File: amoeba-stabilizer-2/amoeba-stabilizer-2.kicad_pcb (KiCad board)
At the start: 2 copper layers, 35.1 x 20.8 mm, 29 parts

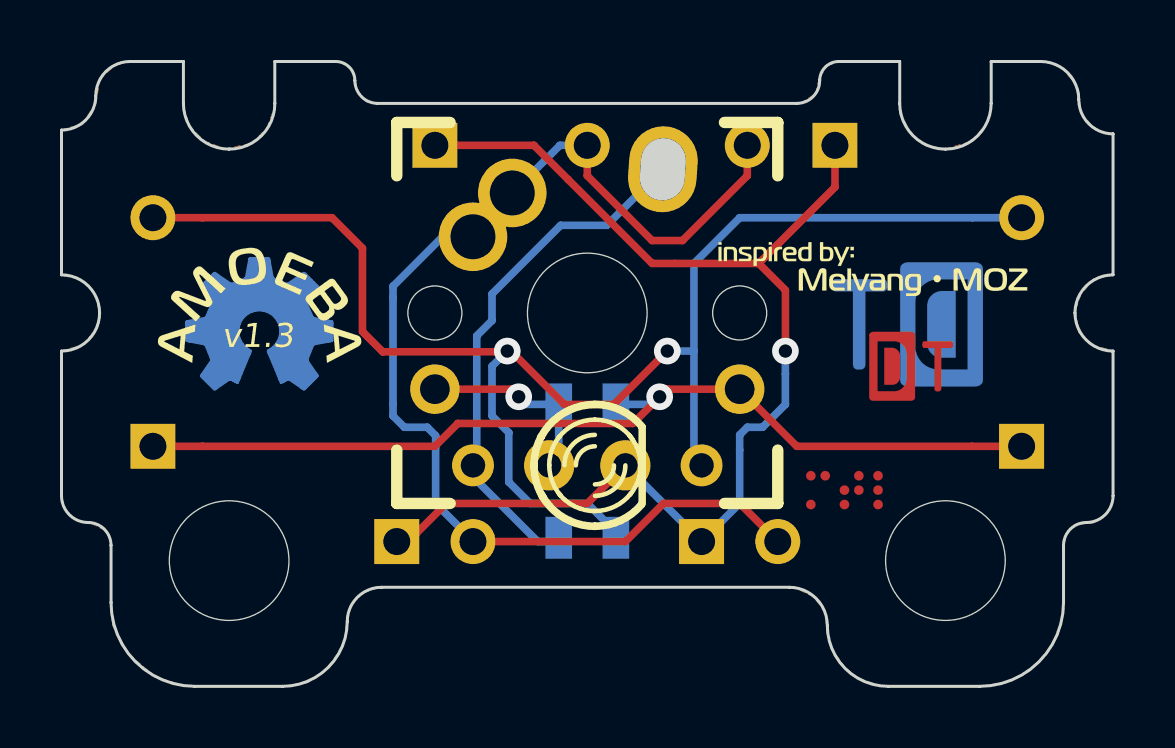
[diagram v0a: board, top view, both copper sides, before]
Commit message: Tighten solder masks, add pad arrows to amoeba-stabilizer-2, convert amoeba on 2u to copper.
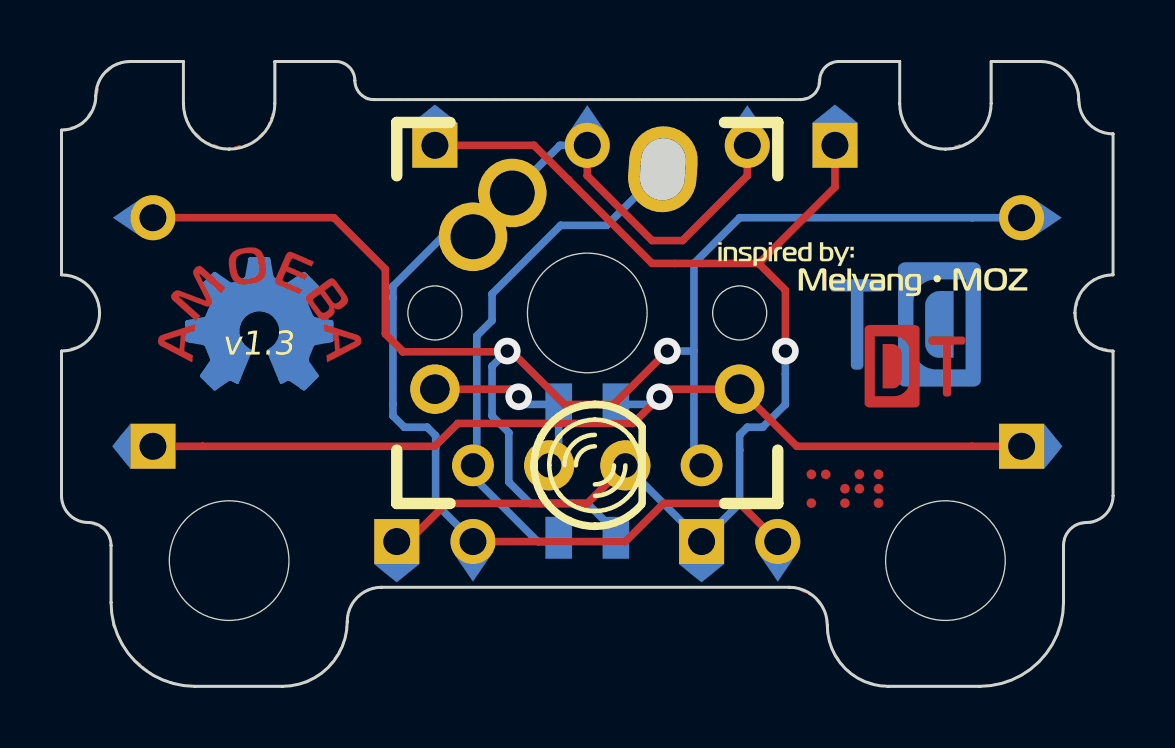
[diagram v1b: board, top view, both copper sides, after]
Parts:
- removed amoeba-round: G***, amoeba-round
- removed dt-logo: G***, dt-logo
- added amoeba-round-cu: G***, amoeba-round-cu, F.Cu at (238.0, 110.2)
- added dt-logo-d: G***, dt-logo-d, F.Cu at (259.1, 112.1)
- added dt-logo-t: G***, dt-logo-t, F.Cu at (260.9, 112.2)
- added pad-arrow-round: G***, pad-arrow-round, B.Cu at (255.3, 118.4)
- added pad-arrow-round: G***, pad-arrow-round, B.Cu at (245.1, 118.4)
- added pad-arrow-round: G***, pad-arrow-round, B.Cu at (234.1, 107.3)
- added pad-arrow-round: G***, pad-arrow-round, B.Cu at (263.7, 107.3)
- added pad-arrow-round: G***, pad-arrow-round, B.Cu at (254.3, 104.6)
- added pad-arrow-round: G***, pad-arrow-round, B.Cu at (248.9, 104.6)
- added pad-arrow-square: G***, pad-arrow-square, B.Cu at (243.8, 104.6)
- added pad-arrow-square: G***, pad-arrow-square, B.Cu at (257.2, 104.6)
- added pad-arrow-square: G***, pad-arrow-square, B.Cu at (263.7, 114.9)
- added pad-arrow-square: G***, pad-arrow-square, B.Cu at (252.7, 118.4)
- added pad-arrow-square: G***, pad-arrow-square, B.Cu at (242.6, 118.4)
- added pad-arrow-square: G***, pad-arrow-square, B.Cu at (234.1, 114.9)
- moved mtl-braille 0.14 mm to (257.4, 116.3)
- moved dt-logo-big-rev 0.06 mm to (259.5, 110.9)
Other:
- outline, holes or cut-outs redrawn

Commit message: Replaced OSH logo.
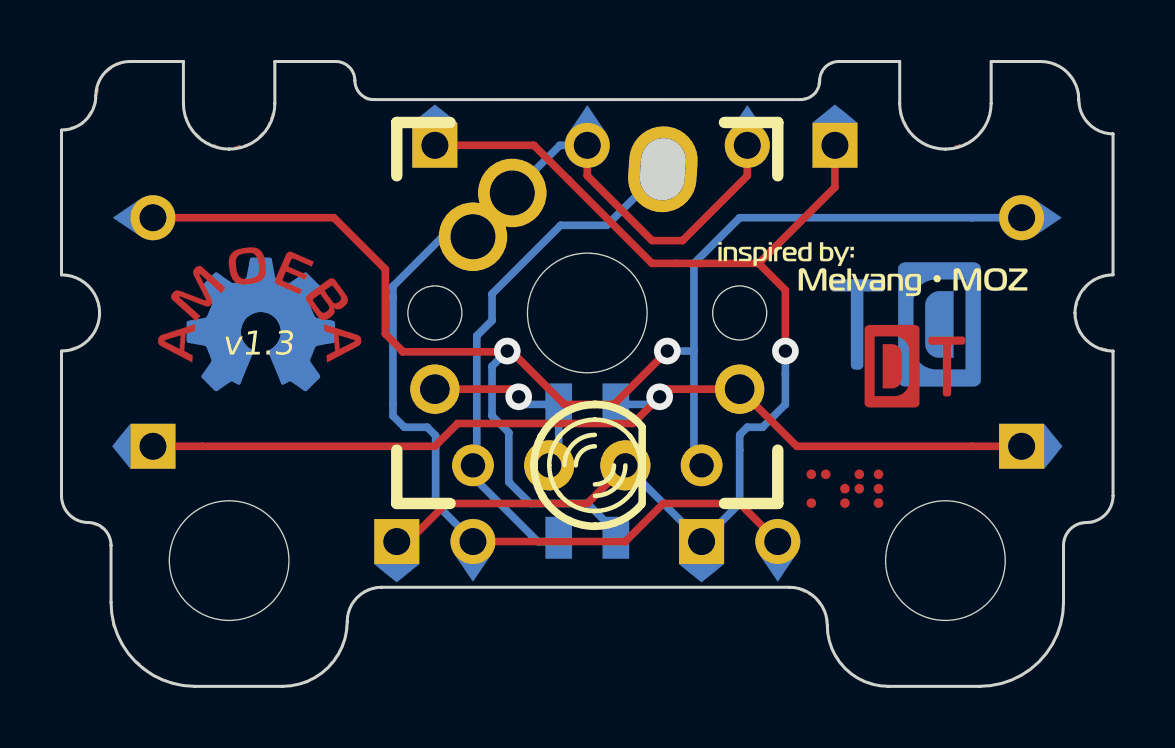
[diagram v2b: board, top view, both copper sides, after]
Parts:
- moved osh-logo-rev 0.06 mm to (238.0, 110.9)

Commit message: Centered amoeba text.
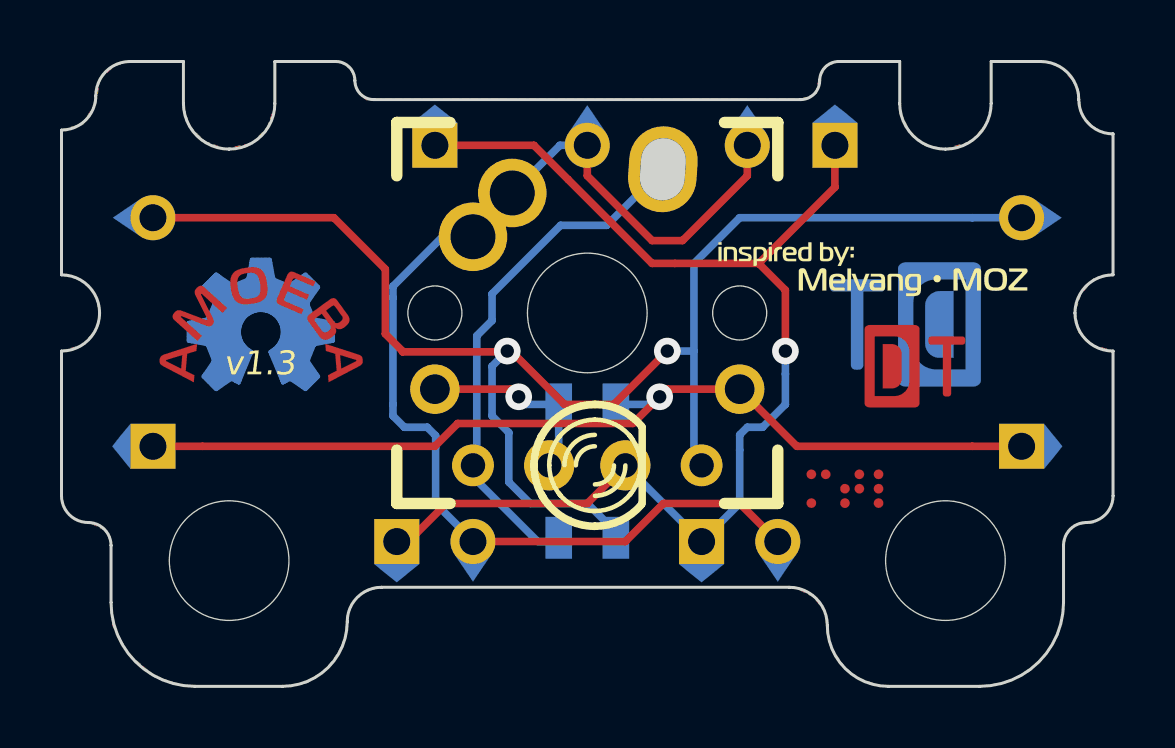
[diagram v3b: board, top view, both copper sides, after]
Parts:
- moved amoeba-round-cu 0.66 mm to (238.0, 110.8)
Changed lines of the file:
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@@
     (20 B.SilkS user)
     (21 F.SilkS user)
-    (22 B.Mask user)
+    (22 B.Mask user hide)
     (23 F.Mask user hide)
     (24 Dwgs.User user hide)
@@
   )
   (module amoeba-round-cu (layer F.Cu)
-    (at 237.998 110.1725)
+    (at 238.0488 110.8329)
     (fp_text reference amoeba-round-cu (at 0 -5.217583) (layer F.SilkS) hide
       (effects (font (size 1.524 1.524) (thickness 0.3048)))
@@
     (effects (font (size 0.8 0.8) (thickness 0.15) italic) (justify mirror))
   )
-  (gr_text v1.3 (at 237.9472 111.506) (layer F.SilkS)
+  (gr_text v1.3 (at 237.998 112.1664) (layer F.SilkS)
     (effects (font (size 0.8 0.8) (thickness 0.12) italic))
   )
@@
     (polygon
       (pts
-        (xy 236.2835 112.141) (xy 236.4105 111.0615) (xy 236.9185 110.363) (xy 237.5916 110.0328) (xy 238.3028 110.0328)
-        (xy 239.0775 110.363) (xy 239.522 110.9345) (xy 239.649 111.76) (xy 239.8395 112.268) (xy 240.0935 112.522)
-        (xy 240.6015 112.522) (xy 241.8715 111.8235) (xy 241.808 110.9345) (xy 241.1095 110.6805) (xy 241.6175 110.109)
-        (xy 240.538 108.7755) (xy 239.649 108.204) (xy 238.6965 107.8865) (xy 237.49 107.8865) (xy 236.2835 108.204)
-        (xy 235.2675 108.966) (xy 234.5055 109.9185) (xy 234.5055 110.2995) (xy 234.8865 110.617) (xy 234.188 110.8075)
-        (xy 234.061 111.8235) (xy 235.458 112.522) (xy 236.0295 112.522)
+        (xy 236.3343 112.8014) (xy 236.4613 111.7219) (xy 236.9693 111.0234) (xy 237.6424 110.6932) (xy 238.3536 110.6932)
+        (xy 239.1283 111.0234) (xy 239.5728 111.5949) (xy 239.6998 112.4204) (xy 239.8903 112.9284) (xy 240.1443 113.1824)
+        (xy 240.6523 113.1824) (xy 241.9223 112.4839) (xy 241.8588 111.5949) (xy 241.1603 111.3409) (xy 241.6683 110.7694)
+        (xy 240.5888 109.4359) (xy 239.6998 108.8644) (xy 238.7473 108.5469) (xy 237.5408 108.5469) (xy 236.3343 108.8644)
+        (xy 235.3183 109.6264) (xy 234.5563 110.5789) (xy 234.5563 110.9599) (xy 234.9373 111.2774) (xy 234.2388 111.4679)
+        (xy 234.1118 112.4839) (xy 235.5088 113.1824) (xy 236.0803 113.1824)
       )
     )
